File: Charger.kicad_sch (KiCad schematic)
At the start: 59 parts, among them Q6 BSC0702LS, Q7 BSC0702LS, Q8 BSC0702LS, Q9 BSC0702LS, U27 BQ25756RRVR

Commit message: Finish v0.2 PCB and DRC
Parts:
- TP1: now not fitted; now left out of the parts list
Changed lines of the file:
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@@
 		(unit 1)
 		(exclude_from_sim no)
-		(in_bom yes)
-		(on_board yes)
-		(dnp no)
+		(in_bom no)
+		(on_board yes)
+		(dnp yes)
 		(property "Reference" "TP1"
 			(at 157.48 248.9201 90)
@@
 				)
 				(hide yes)
-			)
-		)
-		(property "MPN" ""
-			(at 154.94 247.65 0)
-			(effects
-				(font
-					(size 1.27 1.27)
-				)
 			)
 		)
@@
 		(at 154.94 257.81 90)
 		(unit 1)
-		(exclude_from_sim yes)
+		(exclude_from_sim no)
 		(in_bom no)
 		(on_board yes)

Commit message: Additional Infos
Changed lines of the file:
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@@
 					(size 1.27 1.27)
 				)
+				(hide yes)
 			)
 		)
@@
 					(size 1.27 1.27)
 				)
+				(hide yes)
 			)
 		)
@@
 					(size 1.27 1.27)
 				)
+				(hide yes)
 			)
 		)
@@
 					(size 1.27 1.27)
 				)
+				(hide yes)
 			)
 		)
@@
 					(size 1.27 1.27)
 				)
+				(hide yes)
 			)
 		)
@@
 					(size 1.27 1.27)
 				)
+				(hide yes)
 			)
 		)
@@
 					(size 1.27 1.27)
 				)
+				(hide yes)
 			)
 		)

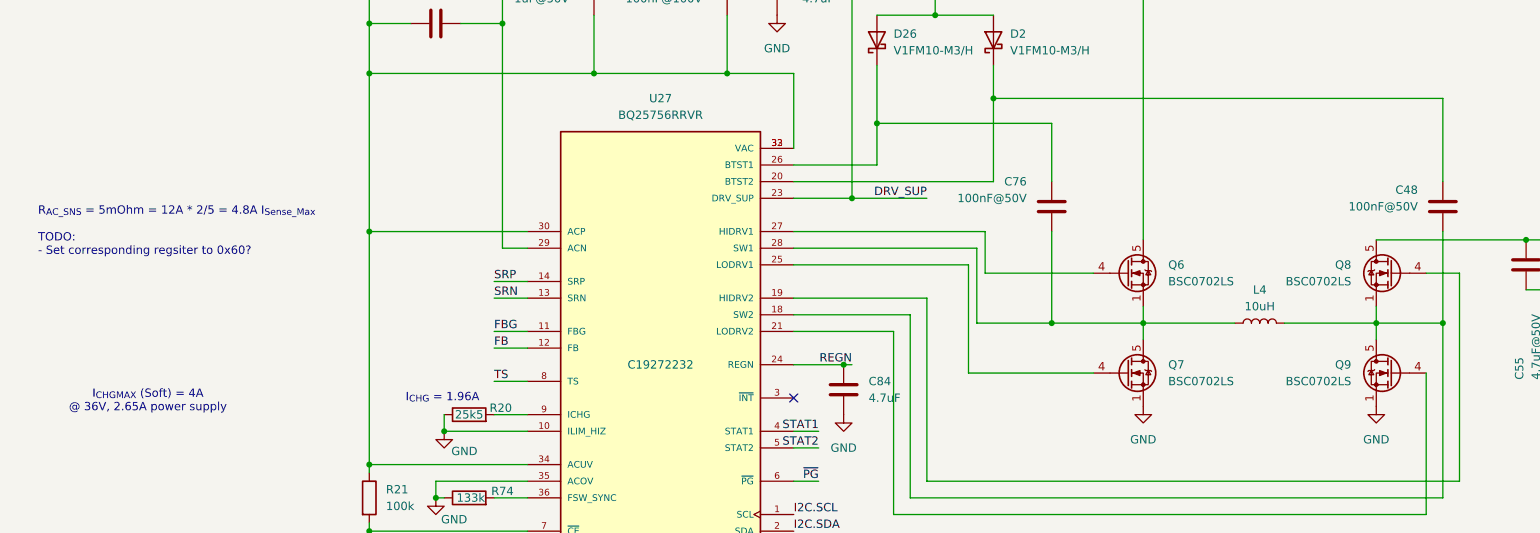
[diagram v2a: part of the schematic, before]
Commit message: 📝 docs(schematic): update component notes and annotations
- update charger schematic text annotations for current limits and thermal considerations
- move and update current sense amplifier circuit notes with design fault details
- add RC filter calculation note for AGPIO2 signal
- update required rework list in main schematic
- reposition components (R38, U44, C88, GND symbols) and associated wiring
- add new components R9 and C94 for AGPIO2 RC filter
- update ERC settings to include undefined netclass error check
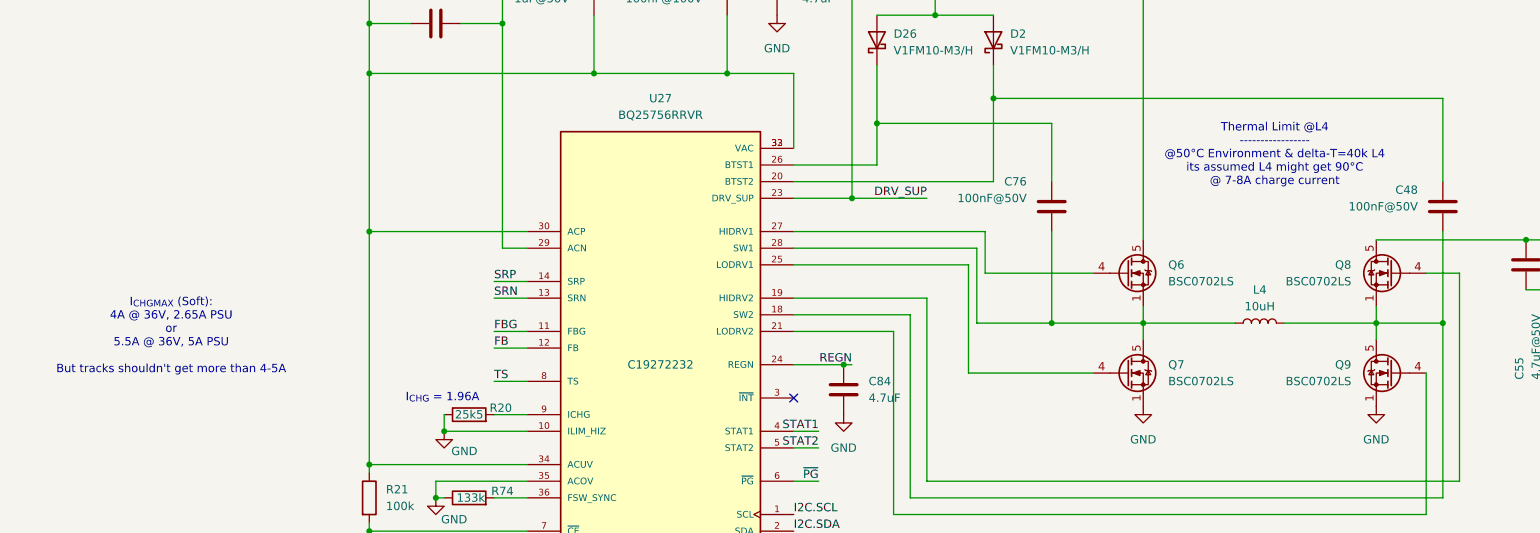
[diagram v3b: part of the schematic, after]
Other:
- note added: "I_{CHG}_{MAX} (Soft): 4A @ 36V, 2.65A PSU or 5.5A @ 36V, 5A PSU But tracks shouldn't get more than 4-5A"
- note added: "Thermal Limit @L4 ----------------- @50°C Environment & delta-T=40k L4 its assumed L4 might get 90°C @ 7-8A charge current"
- note removed: "I_{CHG}_{MAX} (Soft) = 4A @ 36V, 2.65A power supply"
- note removed: "R_{AC_SNS} = 5mOhm = 12A * 2/5 = 4.8A I_{Sense_Max} TODO: - Set corresponding regsiter to 0x60?"
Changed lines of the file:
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@@
 		(comment 1 "This design is licensed under CC BY-NC 4.0")
 	)
-	(text "I_{CHG}_{MAX} (Soft) = 4A\n@ 36V, 2.65A power supply"
+	(text "I_{CHG}_{MAX} (Soft):\n4A @ 36V, 2.65A PSU\nor\n5.5A @ 36V, 5A PSU\n\nBut tracks shouldn't get more than 4-5A"
 		(exclude_from_sim no)
-		(at 32.258 156.718 0)
+		(at 35.814 146.812 0)
 		(effects
 			(font
@@
 		)
 	)
+	(text "Thermal Limit @L4\n-----------------\n@50°C Environment & delta-T=40k L4\nits assumed L4 might get 90°C\n@ 7-8A charge current"
+		(exclude_from_sim no)
+		(at 204.216 119.126 0)
+		(effects
+			(font
+				(size 1.27 1.27)
+			)
+		)
+	)
 	(text "R_{BOTCALC} = 13.76 kOhms = 29.4 V_{CHARGE}\n\nV_{BAT} = 1,536*(1+(R_{TOP}/(R_{BOT}-33)))\n\n7S3P INR18650-13L LiIon:\n- 21.0? V_{EMPTY}, 25.2 V_{NOM}, 29.4 V_{CHARGE}\n- 98.28 Wh, 3.9 Ah\n- 1.95A I_{CHARGE-TYP}, 3.9A I_{CHARGE-MAX}"
 		(exclude_from_sim no)
@@
 		(effects
 			(font
-				(size 1.27 1.27)
-			)
-			(justify left)
-		)
-	)
-	(text "R_{AC_SNS} = 5mOhm = 12A * 2/5 = 4.8A I_{Sense_Max}\n\nTODO:\n- Set corresponding regsiter to 0x60?"
-		(exclude_from_sim no)
-		(at 15.494 130.81 0)
-		(effects
-			(font
